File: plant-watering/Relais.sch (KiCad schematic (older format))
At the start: 12 parts, among them K1 SRD-05VDC-SL-C, K2 SRD-05VDC-SL-C, K3 SRD-05VDC-SL-C, K4 SRD-05VDC-SL-C, K5 SRD-05VDC-SL-C, K6 SRD-05VDC-SL-C

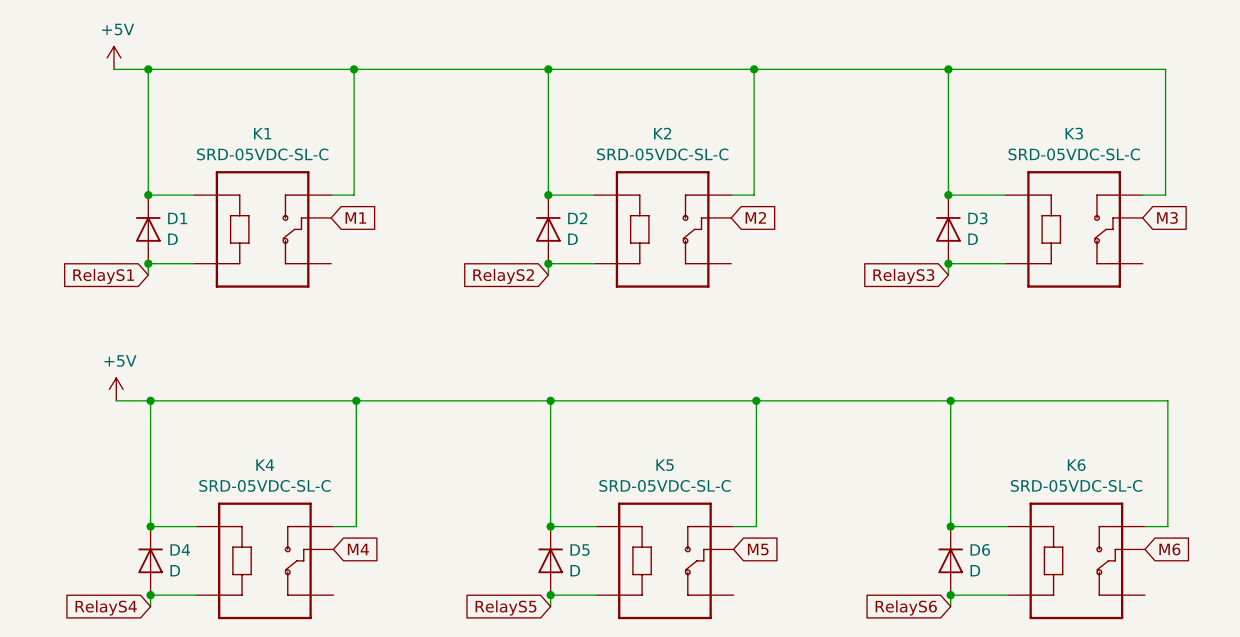
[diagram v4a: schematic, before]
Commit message: changed pcb parts
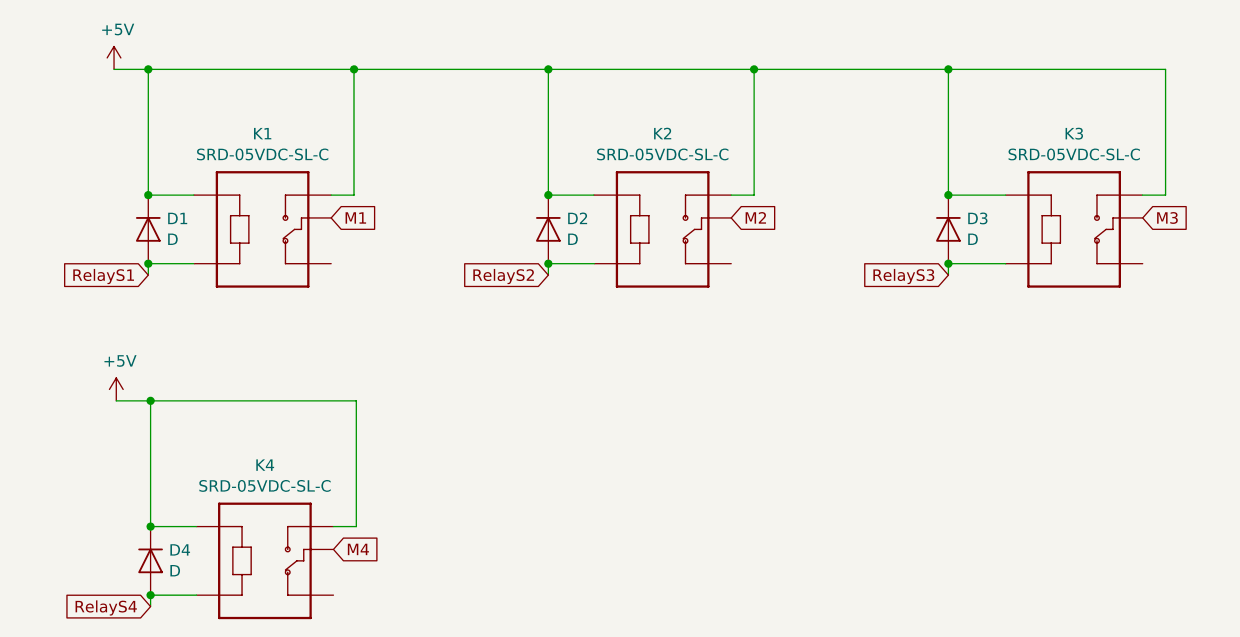
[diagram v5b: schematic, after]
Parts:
- removed D5, D6: D, Diodes_ThroughHole:D_DO-41_SOD81_P7.62mm_Horizontal, symbol Device:D
- removed K5, K6: SRD-05VDC-SL-C, SRD-05VDC-SL-C:RELAY_SRD-05VDC-SL-C, symbol plant-watering-rescue:SRD-05VDC-SL-C-SRD-05VDC-SL-C
- D1, D2, D3, D4: footprint Diodes_ThroughHole:D_DO-41_SOD81_P7.62mm_Horizontal -> Diode_THT:D_DO-41_SOD81_P7.62mm_Horizontal
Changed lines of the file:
@@
 F 0 "D1" V 3704 3530 50  0000 L CNN
 F 1 "D" V 3795 3530 50  0000 L CNN
-F 2 "Diodes_ThroughHole:D_DO-41_SOD81_P7.62mm_Horizontal" H 3750 3450 50  0001 C CNN
+F 2 "Diode_THT:D_DO-41_SOD81_P7.62mm_Horizontal" H 3750 3450 50  0001 C CNN
 F 3 "~" H 3750 3450 50  0001 C CNN
 	1    3750 3450
@@
 F 0 "D2" V 5454 3530 50  0000 L CNN
 F 1 "D" V 5545 3530 50  0000 L CNN
-F 2 "Diodes_ThroughHole:D_DO-41_SOD81_P7.62mm_Horizontal" H 5500 3450 50  0001 C CNN
+F 2 "Diode_THT:D_DO-41_SOD81_P7.62mm_Horizontal" H 5500 3450 50  0001 C CNN
 F 3 "~" H 5500 3450 50  0001 C CNN
 	1    5500 3450
@@
 F 0 "D3" V 7204 3530 50  0000 L CNN
 F 1 "D" V 7295 3530 50  0000 L CNN
-F 2 "Diodes_ThroughHole:D_DO-41_SOD81_P7.62mm_Horizontal" H 7250 3450 50  0001 C CNN
+F 2 "Diode_THT:D_DO-41_SOD81_P7.62mm_Horizontal" H 7250 3450 50  0001 C CNN
 F 3 "~" H 7250 3450 50  0001 C CNN
 	1    7250 3450
@@
 Text GLabel 4560 4850 2    50   Input ~ 0
 M4
-Text GLabel 6310 4850 2    50   Input ~ 0
-M5
-Text GLabel 8110 4850 2    50   Input ~ 0
-M6
 Text GLabel 3760 5100 0    50   Input ~ 0
 RelayS4
-Text GLabel 5510 5100 0    50   Input ~ 0
-RelayS5
-Text GLabel 7260 5100 0    50   Input ~ 0
-RelayS6
 $Comp
 L Device:D D4
@@
 F 0 "D4" V 3714 4980 50  0000 L CNN
 F 1 "D" V 3805 4980 50  0000 L CNN
-F 2 "Diodes_ThroughHole:D_DO-41_SOD81_P7.62mm_Horizontal" H 3760 4900 50  0001 C CNN
+F 2 "Diode_THT:D_DO-41_SOD81_P7.62mm_Horizontal" H 3760 4900 50  0001 C CNN
 F 3 "~" H 3760 4900 50  0001 C CNN
 	1    3760 4900
 	0    1    1    0
 $EndComp
-$Comp
-L Device:D D5
-U 1 1 60114320
-P 5510 4900
-F 0 "D5" V 5464 4980 50  0000 L CNN
-F 1 "D" V 5555 4980 50  0000 L CNN
-F 2 "Diodes_ThroughHole:D_DO-41_SOD81_P7.62mm_Horizontal" H 5510 4900 50  0001 C CNN
-F 3 "~" H 5510 4900 50  0001 C CNN
-	1    5510 4900
-	0    1    1    0
-$EndComp
-$Comp
-L Device:D D6
-U 1 1 60114326
-P 7260 4900
-F 0 "D6" V 7214 4980 50  0000 L CNN
-F 1 "D" V 7305 4980 50  0000 L CNN
-F 2 "Diodes_ThroughHole:D_DO-41_SOD81_P7.62mm_Horizontal" H 7260 4900 50  0001 C CNN
-F 3 "~" H 7260 4900 50  0001 C CNN
-	1    7260 4900
-	0    1    1    0
-$EndComp
 Wire Wire Line
 	3760 5050 3760 5100
-Wire Wire Line
-	5510 5050 5510 5100
-Wire Wire Line
-	7260 5050 7260 5100
 Connection ~ 3760 4200
 Wire Wire Line
 	3760 4200 3610 4200
-Connection ~ 5510 4200
-Connection ~ 7260 4200
 $Comp
 L plant-watering-rescue:SRD-05VDC-SL-C-SRD-05VDC-SL-C K?
@@
 Wire Wire Line
 	3760 4200 4660 4200
-$Comp
-L plant-watering-rescue:SRD-05VDC-SL-C-SRD-05VDC-SL-C K?
-U 1 1 6011433F
-P 6010 4850
-AR Path="/6011433F" Ref="K?"  Part="1"
-AR Path="/600A014F/6011433F" Ref="K5"  Part="1"
-F 0 "K5" H 6010 5217 50  0000 C CNN
-F 1 "SRD-05VDC-SL-C" H 6010 5126 50  0000 C CNN
-F 2 "SRD-05VDC-SL-C:RELAY_SRD-05VDC-SL-C" H 6010 4850 50  0001 L BNN
-F 3 "" H 6010 4850 50  0001 L BNN
-F 4 "IPC-7251" H 6010 4850 50  0001 L BNN "STANDARD"
-F 5 "SONGLE RELAY" H 6010 4850 50  0001 L BNN "MANUFACTURER"
-	1    6010 4850
-	1    0    0    -1
-$EndComp
-$Comp
-L plant-watering-rescue:SRD-05VDC-SL-C-SRD-05VDC-SL-C K?
-U 1 1 60114347
-P 7810 4850
-AR Path="/60114347" Ref="K?"  Part="1"
-AR Path="/600A014F/60114347" Ref="K6"  Part="1"
-F 0 "K6" H 7810 5217 50  0000 C CNN
-F 1 "SRD-05VDC-SL-C" H 7810 5126 50  0000 C CNN
-F 2 "SRD-05VDC-SL-C:RELAY_SRD-05VDC-SL-C" H 7810 4850 50  0001 L BNN
-F 3 "" H 7810 4850 50  0001 L BNN
-F 4 "IPC-7251" H 7810 4850 50  0001 L BNN "STANDARD"
-F 5 "SONGLE RELAY" H 7810 4850 50  0001 L BNN "MANUFACTURER"
-	1    7810 4850
-	1    0    0    -1
-$EndComp
-Wire Wire Line
-	7260 4200 7260 4750
-Wire Wire Line
-	5510 4200 6410 4200
-Wire Wire Line
-	5510 4200 5510 4750
 Wire Wire Line
 	3960 4750 3760 4750
@@
 Wire Wire Line
 	4660 4750 4660 4200
-Connection ~ 4660 4200
-Wire Wire Line
-	4660 4200 5510 4200
-Wire Wire Line
-	6310 4750 6410 4750
-Wire Wire Line
-	6410 4750 6410 4200
-Connection ~ 6410 4200
-Wire Wire Line
-	6410 4200 7260 4200
-Wire Wire Line
-	7510 4750 7260 4750
-Connection ~ 7260 4750
-Wire Wire Line
-	7510 5050 7260 5050
-Connection ~ 7260 5050
-Wire Wire Line
-	8110 4750 8210 4750
-Wire Wire Line
-	8210 4750 8210 4200
-Wire Wire Line
-	8210 4200 7260 4200
-Wire Wire Line
-	5710 5050 5510 5050
-Connection ~ 5510 5050
-Wire Wire Line
-	5710 4750 5510 4750
-Connection ~ 5510 4750
 $EndSCHEMATC
